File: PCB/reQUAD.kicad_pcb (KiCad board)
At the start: 2 copper layers, 51.3 x 18.3 mm, 9 parts, among them J1 Model_100_System_BUS, U1 628128, U2 74573, U3 742G79, U4 7402

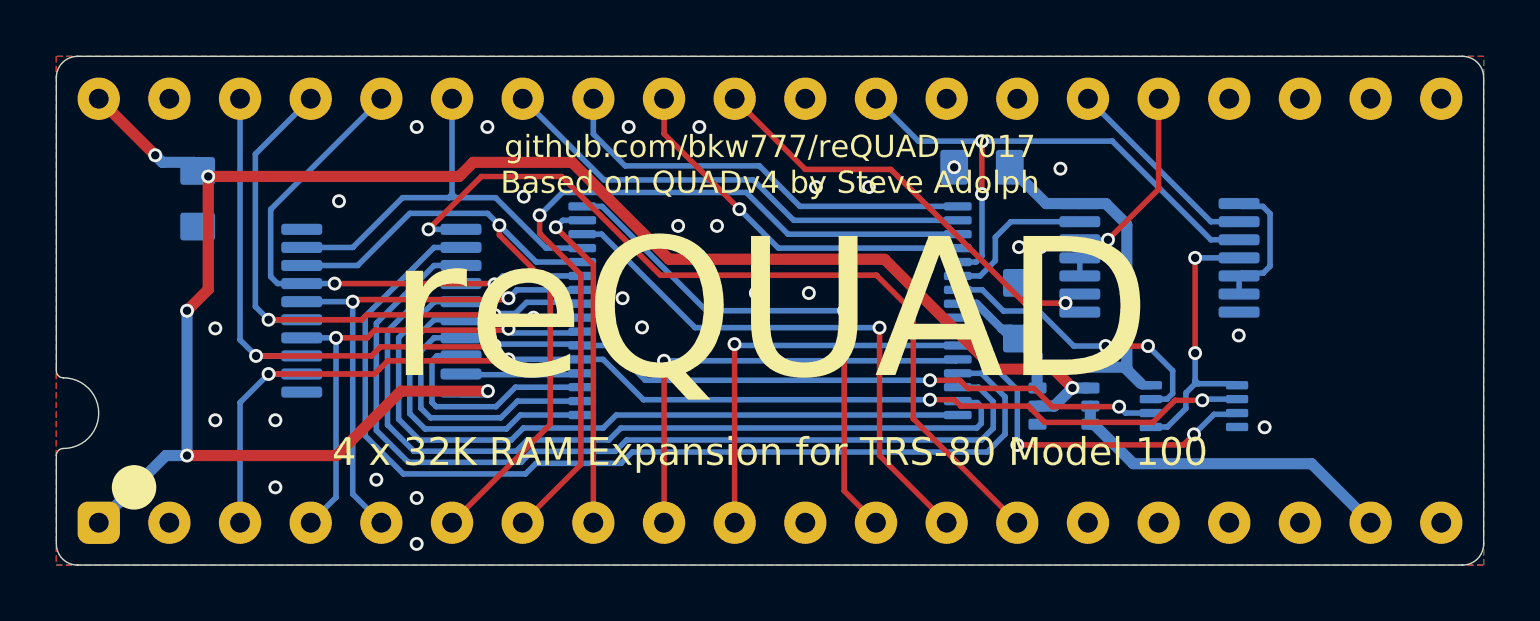
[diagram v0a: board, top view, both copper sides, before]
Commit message: volotile latches, battery
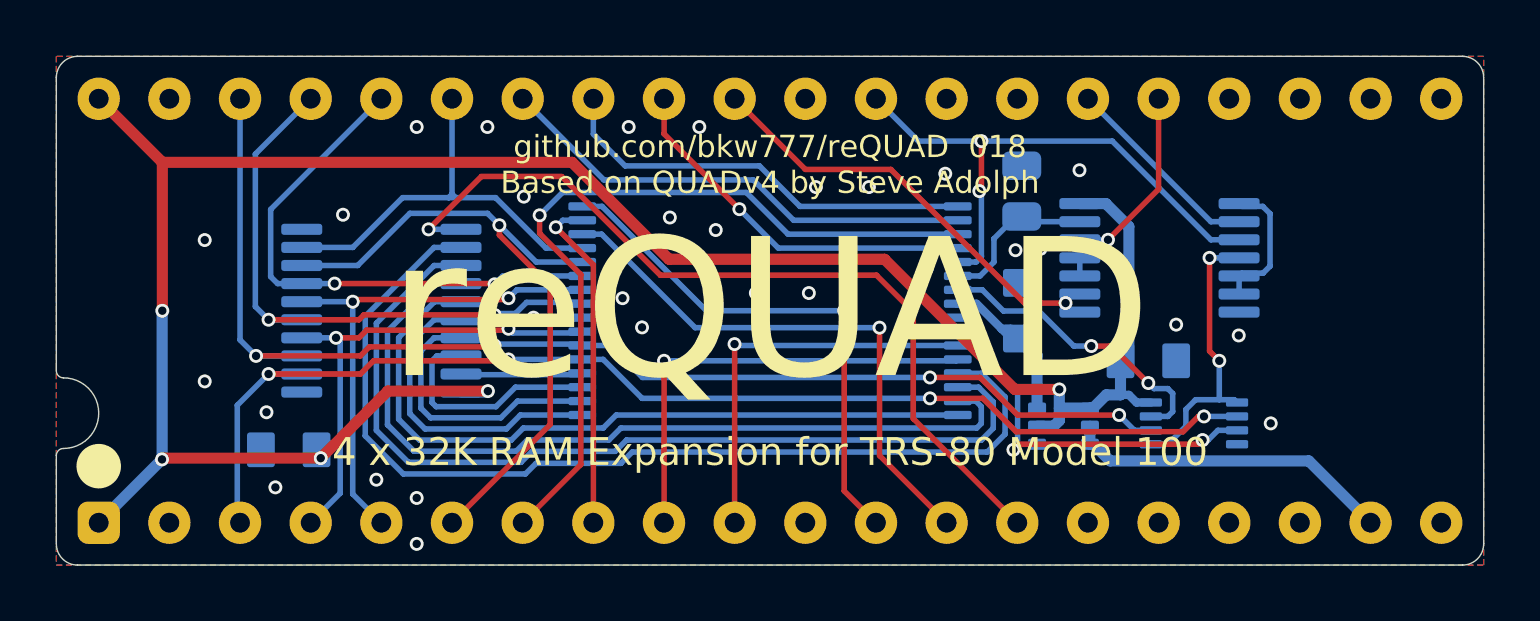
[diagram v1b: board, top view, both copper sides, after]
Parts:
- removed D1: BAV70S, 000_LOCAL:SOT-363_symmetric
- added DA1: BAV70S, 000_LOCAL:SOT-363_symmetric, B.Cu at (160.6, 104.2)
- added R1: 500k, 000_LOCAL:R_0805, B.Cu at (159.1, 95.7)
- C1, C2: value 1u -> 0.1u
- C3: value 47u -> 0.1u
- U1: value 628128 -> AS6C1008
- U2: value 74573 -> 74x573
- U3: value 742G79 -> 74x2G79
- U4: value 7402 -> 74x02
- moved C2 9.60 mm to (132.7, 105.0), turned to 180 degrees
- moved C3 9.17 mm to (163.6, 101.8), turned to 0 degrees
- moved U3 0.62 mm to (165.2, 104.0)
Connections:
- net /ALE* renamed /ALE
- net /FLOP_CLK renamed /BANK_LATCH
- net /IO/~{M}* renamed /IO/~{M}
- net /RESET* renamed /RESET
- net /SRAM_CE2 renamed /RAM_CE2
- net /~{RD}* renamed /~{RD}
- net /~{WR}* renamed /~{WR}
- C2 pad 1: VCC -> VBUS
- C3 pad 1: VMEM -> VBUS
- J1 pad 1: VCC -> VBUS
- J1 pad 40: VCC -> VBUS
- U2 pad 20: VCC -> VBUS
- U3 pad 8: VMEM -> VBUS
- U4 pad 14: VMEM -> VBUS
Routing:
- net VBUS: track 0.00 -> 81.1 mm, vias 0 -> 5
- net VCC: track 69.1 -> 0.00 mm, vias 6 -> 0
- net VMEM: track 20.2 -> 6.34 mm
- net GND: vias 29 -> 30
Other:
- board text added: "github.com/bkw777/reQUAD ${REVISION} Based on QUADv4 by Steve Adolph"
- board text removed: "github.com/bkw777/reQUAD v${REVISION} Based on QUADv4 by Steve Adolph"

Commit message: datasheets
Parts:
- added F1: Fiducial_0.75_1.5, 000_LOCAL:Fiducial_0.75_1.5, B.Cu at (174.3, 94.8)
- added REF**: Fiducial_0.75_1.5, 000_LOCAL:Fiducial_0.75_1.5, B.Cu at (125.7, 94.8)
- added REF**: Fiducial_0.75_1.5, 000_LOCAL:Fiducial_0.75_1.5, B.Cu at (174.3, 105.2)
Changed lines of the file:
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@@
   (title_block
     (title "reQUAD")
-    (date "2023-09-23")
+    (date "2023-09-25")
     (rev "018")
     (company "Brian K. White - b.kenyon.w@gmail.com")
@@
     )
     (pad_to_mask_clearance 0)
-    (solder_mask_min_width 0.22)
-    (allow_soldermask_bridges_in_footprints yes)
     (grid_origin 150 100)
     (pcbplotparams
@@
       (net 19 "VBUS") (pinfunction "VCC") (pintype "power_out"))
     (pad "2" thru_hole circle (at -21.59 7.62 270) (size 1.524 1.524) (drill 0.7112) (layers "*.Cu" "*.Mask")
-      (net 1 "GND") (pinfunction "GND") (pintype "power_out"))
+      (net 1 "GND") (pinfunction "GND") (pintype "power_out") (zone_connect 1) (thermal_bridge_width 0.3) (thermal_gap 0.25))
     (pad "3" thru_hole circle (at -19.05 7.62 270) (size 1.524 1.524) (drill 0.7112) (layers "*.Cu" "*.Mask")
       (net 18 "/AD0") (pinfunction "AD0") (pintype "bidirectional"))
@@
       (net 10 "/A14") (pinfunction "A14") (pintype "output"))
     (pad "11" thru_hole circle (at 1.27 7.62 270) (size 1.524 1.524) (drill 0.7112) (layers "*.Cu" "*.Mask")
-      (net 1 "GND") (pinfunction "GND") (pintype "passive"))
+      (net 1 "GND") (pinfunction "GND") (pintype "passive") (zone_connect 1) (thermal_bridge_width 0.3) (thermal_gap 0.25))
     (pad "12" thru_hole circle (at 3.81 7.62 270) (size 1.524 1.524) (drill 0.7112) (layers "*.Cu" "*.Mask")
       (net 39 "/~{RD}") (pinfunction "~{RD}") (pintype "output"))
@@
       (net 21 "unconnected-(J1-INTR-Pad17)") (pinfunction "INTR") (pintype "input+no_connect"))
     (pad "18" thru_hole circle (at 19.05 7.62 270) (size 1.524 1.524) (drill 0.7112) (layers "*.Cu" "*.Mask")
-      (net 1 "GND") (pinfunction "GND") (pintype "passive"))
+      (net 1 "GND") (pinfunction "GND") (pintype "passive") (zone_connect 1) (thermal_bridge_width 0.3) (thermal_gap 0.25))
     (pad "19" thru_hole circle (at 21.59 7.62 270) (size 1.524 1.524) (drill 0.7112) (layers "*.Cu" "*.Mask")
       (net 43 "/RAM_RST") (pinfunction "RAM_RST") (pintype "output"))
@@
       (net 33 "unconnected-(J1-NC-Pad22)") (pinfunction "NC") (pintype "no_connect"))
     (pad "23" thru_hole circle (at 19.05 -7.62 270) (size 1.524 1.524) (drill 0.7112) (layers "*.Cu" "*.Mask")
-      (net 1 "GND") (pinfunction "GND") (pintype "passive"))
+      (net 1 "GND") (pinfunction "GND") (pintype "passive") (zone_connect 1) (thermal_bridge_width 0.3) (thermal_gap 0.25))
     (pad "24" thru_hole circle (at 16.51 -7.62 270) (size 1.524 1.524) (drill 0.7112) (layers "*.Cu" "*.Mask")
       (net 34 "unconnected-(J1-~{INTA}-Pad24)") (pinfunction "~{INTA}") (pintype "output+no_connect"))
@@
       (net 48 "/~{WR}") (pinfunction "~{WR}") (pintype "output"))
     (pad "30" thru_hole circle (at 1.27 -7.62 270) (size 1.524 1.524) (drill 0.7112) (layers "*.Cu" "*.Mask")
-      (net 1 "GND") (pinfunction "GND") (pintype "passive"))
+      (net 1 "GND") (pinfunction "GND") (pintype "passive") (zone_connect 1) (thermal_bridge_width 0.3) (thermal_gap 0.25))
     (pad "31" thru_hole circle (at -1.27 -7.62 270) (size 1.524 1.524) (drill 0.7112) (layers "*.Cu" "*.Mask")
       (net 37 "/BUS_A15") (pinfunction "A15") (pintype "output"))
@@
       (net 2 "/AD1") (pinfunction "AD1") (pintype "bidirectional"))
     (pad "39" thru_hole circle (at -21.59 -7.62 270) (size 1.524 1.524) (drill 0.7112) (layers "*.Cu" "*.Mask")
-      (net 1 "GND") (pinfunction "GND") (pintype "passive"))
+      (net 1 "GND") (pinfunction "GND") (pintype "passive") (zone_connect 1) (thermal_bridge_width 0.3) (thermal_gap 0.25))
     (pad "40" thru_hole circle (at -24.13 -7.62 270) (size 1.524 1.524) (drill 0.7112) (layers "*.Cu" "*.Mask")
       (net 19 "VBUS") (pinfunction "VCC") (pintype "passive"))
@@
     )
   )
+  (footprint "000_LOCAL:Fiducial_0.75_1.5" (layer "B.Cu")
+    (at 125.7 94.75)
+    (descr "Circular Fiducial, 0.75mm bare copper, 1.5mm soldermask opening (Level B)")
+    (tags "fiducial")
+    (zone_connect 0)
+    (attr board_only exclude_from_pos_files exclude_from_bom)
+    (fp_text reference "REF**" (at 0 2 180) (layer "B.SilkS") hide
+        (effects (font (size 1 1) (thickness 0.15)) (justify mirror))
+    )
+    (fp_text value "Fiducial_0.75_1.5" (at 0 -2 180) (layer "B.Fab") hide
+        (effects (font (size 1 1) (thickness 0.15)) (justify mirror))
+    )
+    (fp_text user "${REFERENCE}" (at 0 0 180) (layer "B.Fab") hide
+        (effects (font (size 0.3 0.3) (thickness 0.05)) (justify mirror))
+    )
+    (fp_circle (center 0 0) (end 1 0)
+      (stroke (width 0.05) (type solid)) (fill none) (layer "B.CrtYd"))
+    (fp_circle (center 0 0) (end 0.75 0)
+      (stroke (width 0.1) (type solid)) (fill none) (layer "B.Fab"))
+    (pad "" smd circle (at 0 0) (size 0.75 0.75) (layers "B.Cu" "B.Mask")
+      (solder_mask_margin 0.375) (clearance 0.375))
+  )
   (footprint "000_LOCAL:SOT-363_symmetric" (layer "B.Cu")
     (at 160.55 104.15 180)
@@
     )
   )
+  (footprint "000_LOCAL:Fiducial_0.75_1.5" (layer "B.Cu")
+    (at 174.3 105.25)
+    (descr "Circular Fiducial, 0.75mm bare copper, 1.5mm soldermask opening (Level B)")
+    (tags "fiducial")
+    (zone_connect 0)
+    (attr board_only exclude_from_pos_files exclude_from_bom)
+    (fp_text reference "REF**" (at 0 2 180) (layer "B.SilkS") hide
+        (effects (font (size 1 1) (thickness 0.15)) (justify mirror))
+    )
+    (fp_text value "Fiducial_0.75_1.5" (at 0 -2 180) (layer "B.Fab") hide
+        (effects (font (size 1 1) (thickness 0.15)) (justify mirror))
+    )
+    (fp_text user "${REFERENCE}" (at 0 0 180) (layer "B.Fab") hide
+        (effects (font (size 0.3 0.3) (thickness 0.05)) (justify mirror))
+    )
+    (fp_circle (center 0 0) (end 1 0)
+      (stroke (width 0.05) (type solid)) (fill none) (layer "B.CrtYd"))
+    (fp_circle (center 0 0) (end 0.75 0)
+      (stroke (width 0.1) (type solid)) (fill none) (layer "B.Fab"))
+    (pad "" smd circle (at 0 0) (size 0.75 0.75) (layers "B.Cu" "B.Mask")
+      (solder_mask_margin 0.375) (clearance 0.375))
+  )
   (footprint "000_LOCAL:C_0805" (layer "B.Cu")
     (at 163.6 101.8)
@@
     )
   )
+  (footprint "000_LOCAL:Fiducial_0.75_1.5" (layer "B.Cu")
+    (at 174.3 94.75)
+    (descr "Circular Fiducial, 0.75mm bare copper, 1.5mm soldermask opening (Level B)")
+    (tags "fiducial")
+    (zone_connect 0)
+    (attr board_only exclude_from_pos_files exclude_from_bom)
+    (fp_text reference "F1" (at 0 2 180) (layer "B.SilkS") hide
+        (effects (font (size 1 1) (thickness 0.15)) (justify mirror))
+    )
+    (fp_text value "Fiducial_0.75_1.5" (at 0 -2 180) (layer "B.Fab") hide
+        (effects (font (size 1 1) (thickness 0.15)) (justify mirror))
+    )
+    (fp_text user "${REFERENCE}" (at 0 0 180) (layer "B.Fab") hide
+        (effects (font (size 0.3 0.3) (thickness 0.05)) (justify mirror))
+    )
+    (fp_circle (center 0 0) (end 1 0)
+      (stroke (width 0.05) (type solid)) (fill none) (layer "B.CrtYd"))
+    (fp_circle (center 0 0) (end 0.75 0)
+      (stroke (width 0.1) (type solid)) (fill none) (layer "B.Fab"))
+    (pad "" smd circle (at 0 0) (size 0.75 0.75) (layers "B.Cu" "B.Mask")
+      (solder_mask_margin 0.375) (clearance 0.375))
+  )
   (gr_circle (center 125.87 105.588) (end 125.47 105.588)
     (stroke (width 0.8) (type solid)) (fill none) (layer "F.SilkS"))
@@
     )
   )
-  (zone (net 1) (net_name "GND") (layer "F.Cu") (hatch edge 0.508)
-    (connect_pads (clearance 0.2))
-    (min_thickness 0.2) (filled_areas_thickness no)
-    (fill yes (thermal_gap 0.2) (thermal_bridge_width 0.3) (smoothing fillet) (radius 0.2))
-    (polygon
-      (pts
-        (xy 124.346 109.144)
-        (xy 175.654 109.144)
-        (xy 175.654 90.856)
-        (xy 124.346 90.856)
-      )
-    )
-  )
   (zone (net 16) (net_name "/AD4") (layer "F.Cu") (name "$teardrop_padvia$") (hatch edge 0.5)
     (priority 30019)
@@
     )
   )
+  (zone (net 1) (net_name "GND") (layers "F&B.Cu") (hatch edge 0.5)
+    (connect_pads yes (clearance 0.2))
+    (min_thickness 0.2) (filled_areas_thickness no)
+    (fill yes (thermal_gap 0.3) (thermal_bridge_width 0.3) (smoothing fillet) (radius 0.1))
+    (polygon
+      (pts
+        (xy 124.346 109.144)
+        (xy 175.654 109.144)
+        (xy 175.654 90.856)
+        (xy 124.346 90.856)
+      )
+    )
+  )
   (zone (net 7) (net_name "/A11") (layer "B.Cu") (name "$teardrop_padvia$") (hatch edge 0.5)
     (priority 30105)
@@
       )
     )
-  )
-  (zone (net 1) (net_name "GND") (layer "B.Cu") (hatch edge 0.508)
-    (connect_pads (clearance 0.2))
-    (min_thickness 0.2) (filled_areas_thickness no)
-    (fill yes (thermal_gap 0.2) (thermal_bridge_width 0.3) (smoothing fillet) (radius 0.2))
-    (polygon
-      (pts
-        (xy 124.346 109.144)
-        (xy 175.654 109.144)
-        (xy 175.654 90.856)
-        (xy 124.346 90.856)
-      )
-    )

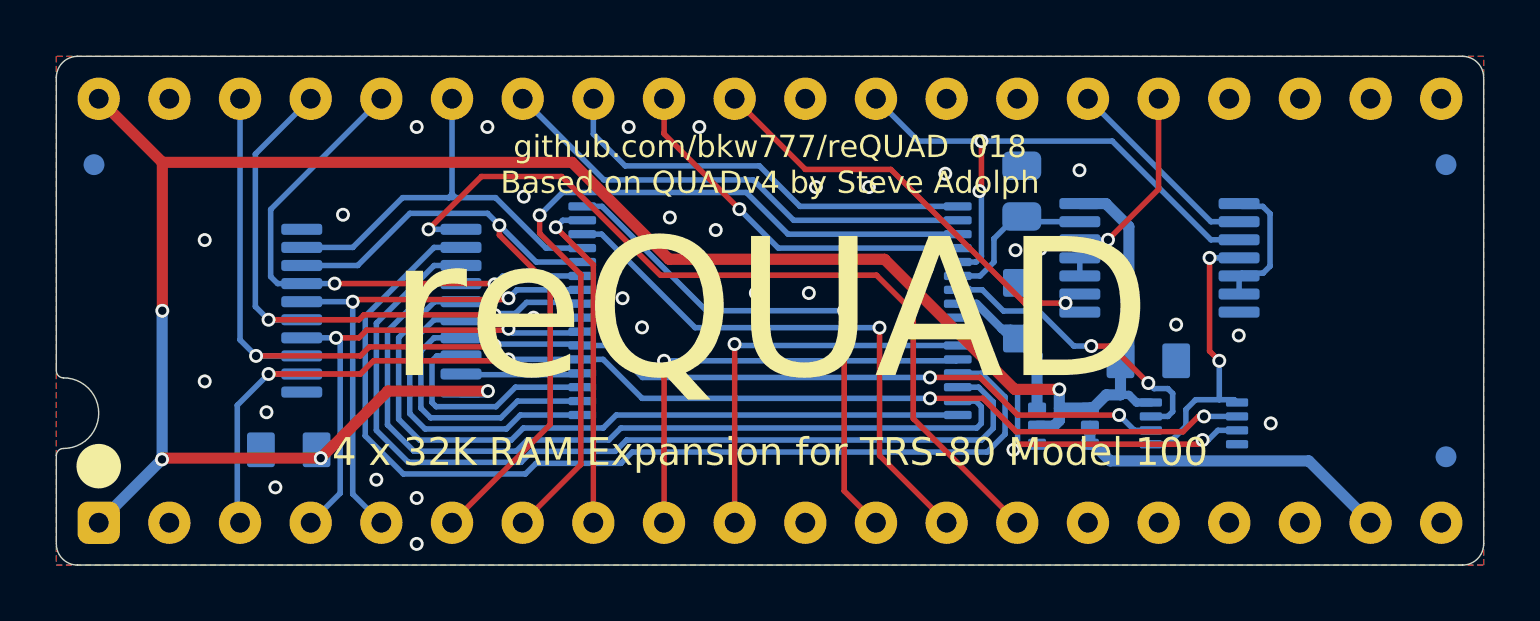
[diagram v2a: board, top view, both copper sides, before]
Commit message: make v020 main even though not tested yet
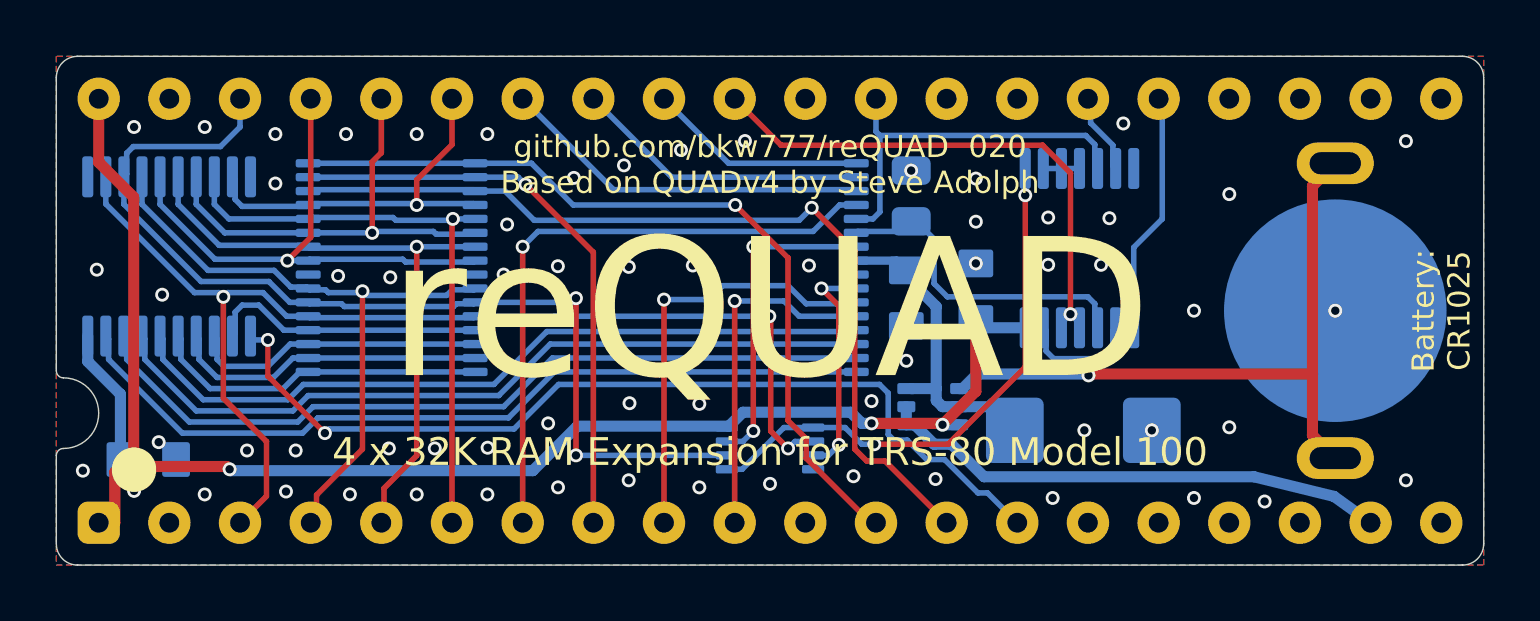
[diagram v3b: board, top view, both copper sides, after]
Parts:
- removed F1, REF** (x2): Fiducial_0.75_1.5, 000_LOCAL:Fiducial_0.75_1.5
- added BT1: Keystone_3031, 000_LOCAL:Keystone_3031, B.Cu at (170.3, 100.0)
- added C4: 220u, 000_LOCAL:CP_EIA-6032-28, B.Cu at (161.3, 104.3)
- C1, C2, C3: value 0.1u -> 1u
- DA1: value BAV70S -> BAV756S; footprint 000_LOCAL:SOT-363_symmetric -> 000_LOCAL:SOT-363
- U1: footprint 000_LOCAL:TSOP32-14mm -> 000_LOCAL:TSOP32-dual
- moved U3 15.3 mm to (150.0, 105.0)
- moved U2 7.88 mm to (128.4, 98.0), turned to -90 degrees
- moved U1 6.93 mm to (143.2, 98.5), turned to 180 degrees
- moved C3 6.69 mm to (157.4, 99.3), turned to 90 degrees
- moved C2 5.06 mm to (127.7, 105.3), turned to 0 degrees
- moved DA1 4.75 mm to (155.8, 103.5)
- moved C1 4.12 mm to (154.9, 99.5), turned to -90 degrees
- moved R1 3.98 mm to (155.1, 95.9)
- moved U4 2.90 mm to (161.1, 97.8), turned to -90 degrees
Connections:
- DA1 pad 1: VBUS -> /BATT+
- DA1 pad 2: /RAM_RST -> VMEM
- DA1 pad 3: /RAM_RST -> VBUS
- DA1 pad 4: unconnected-(DA1B-A-Pad4) -> /RAM_RST
- DA1 pad 5: VBUS -> /RAM_RST
- U1 pad 1: /A11 -> /A13
- U1 pad 11: /A14 -> /A12
- U1 pad 12: /A12 -> /A14
- U1 pad 13: /A7 -> /A3
- U1 pad 14: /A6 -> /A2
- U1 pad 15: /A5 -> /A1
- U1 pad 16: /A4 -> /A0
- U1 pad 17: /A3 -> /A4
- U1 pad 18: /A2 -> /A5
- U1 pad 19: /A1 -> /A6
- U1 pad 2: /A9 -> /A11
- U1 pad 20: /A0 -> /A7
- U1 pad 3: /A8 -> /A9
- U1 pad 4: /A13 -> /A8
- U1 pad 9: unconnected-(U1-NC-Pad9) -> GND
- U4 pad 1: Net-(U4-Pad1) -> /BANK_LATCH
- U4 pad 10: Net-(U4-Pad10) -> /RAM_CE2
- U4 pad 11: Net-(U4-Pad10) -> /BUS_A15
- U4 pad 12: /RESET -> /BUS_A15
- U4 pad 13: /RAM_CE2 -> Net-(U4-Pad13)
- U4 pad 2: /~{Y0} -> Net-(U4-Pad2)
- U4 pad 3: /~{WR} -> Net-(U4-Pad2)
- U4 pad 4: /BANK_LATCH -> Net-(U4-Pad2)
- U4 pad 5: Net-(U4-Pad1) -> /~{WR}
- U4 pad 6: Net-(U4-Pad1) -> /~{Y0}
- U4 pad 8: /BUS_A15 -> /RESET
- U4 pad 9: /BUS_A15 -> Net-(U4-Pad13)
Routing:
- net /A7: track 36.3 -> 10.0 mm
- net /A0: track 4.39 -> 29.8 mm
- net /BATT+: track 0.00 -> 24.2 mm, vias 0 -> 1
- net /A6: track 33.4 -> 10.6 mm
- net VBUS: track 81.1 -> 58.7 mm
- net /A1: track 8.37 -> 29.0 mm
- net /A5: track 30.4 -> 11.4 mm
- net /A2: track 9.88 -> 28.2 mm
- net /A3: track 11.3 -> 27.4 mm
- net /A4: track 26.5 -> 12.1 mm
- net /IO/~{M}: track 20.1 -> 32.5 mm
- net /~{RD}: track 19.1 -> 29.6 mm
- net /BANK_LATCH: track 10.5 -> 19.9 mm
- net /A10: track 12.2 -> 21.1 mm
- net /AD1: track 44.8 -> 36.3 mm, vias 4 -> 2
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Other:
- board text added: "Battery: CR1025"
